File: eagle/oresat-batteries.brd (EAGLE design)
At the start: 94 x 93.5 mm, 62 parts, among them IC1 74AHC1G08DBV, U1 TCAN330, U2 STM32F042K6, X1 16MHz

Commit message: More cleaning.
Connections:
- removed net N$4: CF1.P$1, D2.3
- new net BATOUT: CF1.P$3, D2.3
- net CANH: now also CF1.P$2; no longer CF1.P$4
- net CANL: now also CF1.P$1; no longer CF1.P$5
- net ISO_S: now also CF1.P$5; no longer CF1.P$2
- net VSOLAR: now also CF1.P$4; no longer CF1.P$3
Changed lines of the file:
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@@
 <wire x1="17.35" y1="76" x2="21.85" y2="81.93" width="0" layer="19" extent="1-1"/>
-</signal>
-<signal name="LEDNP">
-<contactref element="R2" pad="2"/>
-<contactref element="LED1" pad="A"/>
-<wire x1="13.35" y1="76" x2="28.5" y2="76.75" width="0" layer="19" extent="1-1"/>
 </signal>
 <signal name="ADP_LED">
@@
 <signal name="ISO_S">
 <contactref element="C3" pad="1"/>
-<contactref element="CF1" pad="P$2"/>
 <contactref element="U$1" pad="9"/>
 <contactref element="U$1" pad="11"/>
 <contactref element="U$1" pad="10"/>
+<contactref element="CF1" pad="P$5"/>
 <wire x1="22.85" y1="78.23" x2="23.7" y2="79.08" width="0" layer="19" extent="1-1"/>
 <wire x1="22.35" y1="78.23" x2="22.85" y2="78.23" width="0" layer="19" extent="1-1"/>
 <wire x1="11.65" y1="73" x2="22.35" y2="78.23" width="0" layer="19" extent="1-1"/>
-<wire x1="9.435" y1="92.04" x2="22.35" y2="78.23" width="0" layer="19" extent="1-1"/>
+<wire x1="11.975" y1="86.96" x2="22.35" y2="78.23" width="0" layer="19" extent="1-1"/>
 </signal>
 <signal name="VSOLAR">
+<contactref element="DEBUG_DNP" pad="7"/>
+<contactref element="DEBUG_DNP" pad="8"/>
 <contactref element="U$1" pad="8"/>
 <contactref element="U$1" pad="6"/>
 <contactref element="U$1" pad="7"/>
-<contactref element="CF1" pad="P$3"/>
 <contactref element="C5" pad="1"/>
-<contactref element="DEBUG_DNP" pad="7"/>
-<contactref element="DEBUG_DNP" pad="8"/>
-<wire x1="21.35" y1="78.23" x2="21.85" y2="78.23" width="0" layer="19" extent="1-1"/>
-<wire x1="20.85" y1="78.23" x2="21.35" y2="78.23" width="0" layer="19" extent="1-1"/>
-<wire x1="10.705" y1="86.96" x2="20.85" y2="78.23" width="0" layer="19" extent="1-1"/>
+<contactref element="CF1" pad="P$4"/>
+<wire x1="20.85" y1="78.23" x2="10.705" y2="92.04" width="0" layer="19" extent="1-1"/>
+<wire x1="21.35" y1="78.23" x2="20.85" y2="78.23" width="0" layer="19" extent="1-1"/>
+<wire x1="21.85" y1="78.23" x2="21.35" y2="78.23" width="0" layer="19" extent="1-1"/>
 <wire x1="19.15" y1="52.5" x2="20.85" y2="78.23" width="0" layer="19" extent="1-1"/>
 <wire x1="0.23" y1="-13.73" x2="19.15" y2="52.5" width="0" layer="19" extent="1-1"/>
@@
 <contactref element="R7" pad="1"/>
 <contactref element="U$2" pad="5"/>
-<contactref element="CF1" pad="P$6"/>
 <contactref element="IC1" pad="1"/>
 <contactref element="R14" pad="2"/>
+<contactref element="CF1" pad="P$6"/>
 <wire x1="15.65" y1="73" x2="26.66" y2="77.875" width="0" layer="19" extent="1-1"/>
 <wire x1="9.35" y1="79" x2="15.65" y2="73" width="0" layer="19" extent="1-1"/>
@@
 <wire x1="16.35" y1="56.5" x2="15" y2="66.75" width="0" layer="19" extent="1-1"/>
 </signal>
-<signal name="N$4">
-<contactref element="CF1" pad="P$1"/>
-<contactref element="D2" pad="3"/>
-<wire x1="15.5" y1="47.4" x2="9.435" y2="86.96" width="0" layer="19" extent="1-1"/>
-</signal>
 <signal name="IO0">
 <contactref element="U$5" pad="1"/>
@@
 <signal name="CANH">
 <contactref element="U1" pad="7"/>
-<contactref element="CF1" pad="P$4"/>
 <contactref element="DEBUG_DNP" pad="14"/>
 <contactref element="DEBUG_DNP" pad="13"/>
-<wire x1="27.175" y1="74.8" x2="10.705" y2="92.04" width="0" layer="19" extent="1-1"/>
+<contactref element="CF1" pad="P$2"/>
+<wire x1="9.435" y1="92.04" x2="27.175" y2="74.8" width="0" layer="19" extent="1-1"/>
 <wire x1="7.85" y1="-13.73" x2="27.175" y2="74.8" width="0" layer="19" extent="1-1"/>
 <wire x1="7.85" y1="-16.27" x2="7.85" y2="-13.73" width="0" layer="19" extent="1-1"/>
@@
 <signal name="CANL">
 <contactref element="U1" pad="6"/>
-<contactref element="CF1" pad="P$5"/>
 <contactref element="DEBUG_DNP" pad="12"/>
 <contactref element="DEBUG_DNP" pad="11"/>
-<wire x1="11.975" y1="86.96" x2="27.825" y2="74.8" width="0" layer="19" extent="1-1"/>
+<contactref element="CF1" pad="P$1"/>
+<wire x1="9.435" y1="86.96" x2="27.825" y2="74.8" width="0" layer="19" extent="1-1"/>
 <wire x1="5.31" y1="-13.73" x2="27.825" y2="74.8" width="0" layer="19" extent="1-1"/>
 <wire x1="5.31" y1="-16.27" x2="5.31" y2="-13.73" width="0" layer="19" extent="1-1"/>
@@
 </signal>
 <signal name="VBATT+">
-<contactref element="U$1" pad="4"/>
-<contactref element="U$1" pad="12"/>
-<contactref element="U$1" pad="13"/>
-<contactref element="U$1" pad="14"/>
 <contactref element="C2" pad="1"/>
 <contactref element="U2" pad="17"/>
@@
 <contactref element="C11" pad="1"/>
 <contactref element="U2" pad="1"/>
-<contactref element="CF2" pad="2"/>
 <contactref element="U1" pad="3"/>
 <contactref element="C13" pad="1"/>
@@
 <contactref element="R7" pad="2"/>
 <contactref element="R10" pad="2"/>
+<contactref element="U$1" pad="4"/>
+<contactref element="U$1" pad="12"/>
+<contactref element="U$1" pad="13"/>
+<contactref element="U$1" pad="14"/>
+<contactref element="CF2" pad="2"/>
 <wire x1="23.7" y1="80.08" x2="23.7" y2="79.58" width="0" layer="19" extent="1-1"/>
 <wire x1="23.7" y1="80.58" x2="23.7" y2="80.08" width="0" layer="19" extent="1-1"/>
@@
 <wire x1="-4.475" y1="-3.435" x2="-3.825" y2="-3.435" width="0" layer="19" extent="1-1"/>
 </signal>
+<signal name="LEDNP">
+<contactref element="R2" pad="2"/>
+<contactref element="LED1" pad="A"/>
+<wire x1="13.35" y1="76" x2="28.5" y2="76.75" width="0" layer="19" extent="1-1"/>
+</signal>
+<signal name="BATOUT">
+<contactref element="D2" pad="3"/>
+<contactref element="CF1" pad="P$3"/>
+<wire x1="15.5" y1="47.4" x2="10.705" y2="86.96" width="0" layer="19" extent="1-1"/>
+</signal>
 </signals>

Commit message: Fixed V- pin on STC
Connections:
- net C_SENSE: no longer R6.2
- net GND: now also R6.2
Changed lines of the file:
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@@
 <contactref element="C14" pad="2"/>
 <contactref element="R3" pad="1"/>
+<contactref element="R6" pad="2"/>
 <wire x1="21.85" y1="80.08" x2="20.85" y2="81.93" width="0" layer="19" extent="1-1"/>
 <wire x1="22.415" y1="75.42" x2="21.85" y2="80.08" width="0" layer="19" extent="1-1"/>
@@
 <wire x1="14.2" y1="66.75" x2="13.35" y2="70" width="0" layer="19" extent="1-1"/>
 <wire x1="11.65" y1="76" x2="13.35" y2="73" width="0" layer="19" extent="1-1"/>
-<wire x1="7.65" y1="73" x2="11.65" y2="76" width="0" layer="19" extent="1-1"/>
+<wire x1="9.35" y1="76" x2="11.65" y2="76" width="0" layer="19" extent="1-1"/>
+<wire x1="7.65" y1="73" x2="9.35" y2="76" width="0" layer="19" extent="1-1"/>
 <wire x1="27.175" y1="72.2" x2="22.415" y2="75.42" width="0" layer="19" extent="1-1"/>
 <wire x1="24.85" y1="68.5" x2="27.175" y2="72.2" width="0" layer="19" extent="1-1"/>
@@
 </signal>
 <signal name="C_SENSE">
-<contactref element="R6" pad="2"/>
 <contactref element="R3" pad="2"/>
 <contactref element="U$13" pad="P$1"/>
@@
 <contactref element="U$13" pad="P$3"/>
 <contactref element="U$5" pad="6"/>
-<wire x1="9.35" y1="76" x2="21.795" y2="75.42" width="0" layer="19" extent="1-1"/>
 <wire x1="29.35" y1="53" x2="21.795" y2="75.42" width="0" layer="19" extent="1-1"/>
 <wire x1="-3.175" y1="-3.435" x2="29.35" y2="53" width="0" layer="19" extent="1-1"/>

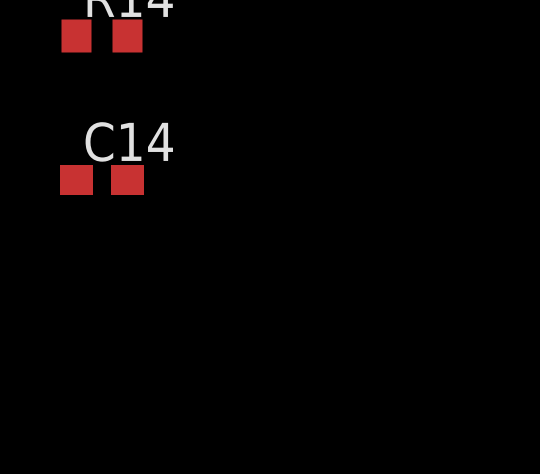
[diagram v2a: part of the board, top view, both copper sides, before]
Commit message: Fixed TP non-connect issue
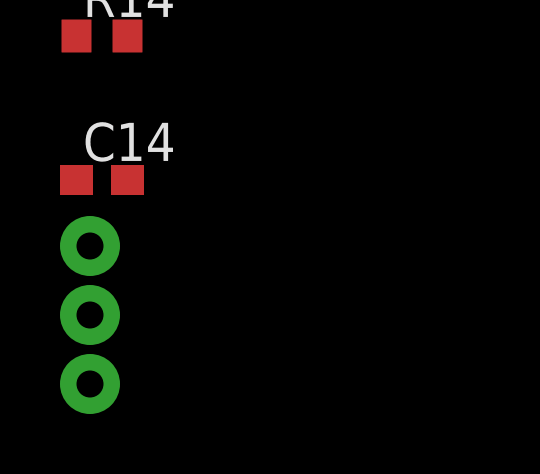
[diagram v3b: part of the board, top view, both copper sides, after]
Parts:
- added U$18, U$19, U$28: TP, oresat-batteries:2MM_TP
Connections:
- net BQBAT: now also U$26.P$1, U$4.P$1
- net CANH: now also U$12.P$1
- net CANL: now also U$8.P$1
- net COUT: now also U$19.P$1
- net C_SENSE: now also U$18.P$1
- net GND: now also U$16.P$1, U$17.P$1, U$22.P$1, U$23.P$1
- net IO0: now also U$9.P$1
- net N$5: now also U$28.P$1
- net NRESET: now also U$25.P$1
- net PA8: now also U$27.P$1
- net SCL: now also U$10.P$1
- net SDA: now also U$11.P$1
- net SYS_EN: now also U$24.P$1
- net VBATT+: now also U$15.P$1, U$7.P$1
- net VSOLAR: now also U$6.P$1
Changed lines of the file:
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@@
 <element name="R14" library="rcl" package="R0603" value="2.2k" x="-29.4" y="-44.6"/>
 <element name="C14" library="rcl" package="C0603" value="" x="-29.4" y="-49.4"/>
+<element name="U$18" library="oresat-batteries" package="2MM_TP" value="TP" x="-29.8" y="-51.6"/>
+<element name="U$19" library="oresat-batteries" package="2MM_TP" value="TP" x="-29.8" y="-53.9"/>
+<element name="U$28" library="oresat-batteries" package="2MM_TP" value="TP" x="-29.8" y="-56.2"/>
 </elements>
 <signals>
@@
 <contactref element="R3" pad="1"/>
 <contactref element="R6" pad="2"/>
+<contactref element="U$22" pad="P$1"/>
+<contactref element="U$23" pad="P$1"/>
+<contactref element="U$16" pad="P$1"/>
+<contactref element="U$17" pad="P$1"/>
 <wire x1="21.85" y1="80.08" x2="20.85" y2="81.93" width="0" layer="19" extent="1-1"/>
 <wire x1="22.415" y1="75.42" x2="21.85" y2="80.08" width="0" layer="19" extent="1-1"/>
@@
 <wire x1="10.39" y1="-13.73" x2="32.5" y2="21" width="0" layer="19" extent="16-16"/>
 <wire x1="10.39" y1="-16.27" x2="10.39" y2="-13.73" width="0" layer="19" extent="1-1"/>
-<wire x1="-26.95" y1="-39.09" x2="10.39" y2="-16.27" width="0" layer="19" extent="1-1"/>
+<wire x1="-8" y1="-9" x2="10.39" y2="-13.73" width="0" layer="19" extent="1-1"/>
+<wire x1="-8" y1="-6.5" x2="-8" y2="-9" width="0" layer="19" extent="1-1"/>
+<wire x1="-21.5" y1="-29" x2="-8" y2="-9" width="0" layer="19" extent="1-1"/>
+<wire x1="-21.5" y1="-31.5" x2="-21.5" y2="-29" width="0" layer="19" extent="1-1"/>
+<wire x1="-26.95" y1="-39.09" x2="-21.5" y2="-31.5" width="0" layer="19" extent="1-1"/>
 <wire x1="-28.55" y1="-49.4" x2="-26.95" y2="-39.09" width="0" layer="19" extent="1-1"/>
 </signal>
@@
 <contactref element="C5" pad="1"/>
 <contactref element="CF1" pad="P$4"/>
+<contactref element="U$6" pad="P$1"/>
 <wire x1="20.85" y1="78.23" x2="10.705" y2="92.04" width="0" layer="19" extent="1-1"/>
 <wire x1="21.35" y1="78.23" x2="20.85" y2="78.23" width="0" layer="19" extent="1-1"/>
 <wire x1="21.85" y1="78.23" x2="21.35" y2="78.23" width="0" layer="19" extent="1-1"/>
-<wire x1="19.15" y1="52.5" x2="20.85" y2="78.23" width="0" layer="19" extent="1-1"/>
+<wire x1="34" y1="66.5" x2="21.85" y2="78.23" width="0" layer="19" extent="1-1"/>
+<wire x1="19.15" y1="52.5" x2="34" y2="66.5" width="0" layer="19" extent="1-1"/>
 <wire x1="0.23" y1="-13.73" x2="19.15" y2="52.5" width="0" layer="19" extent="1-1"/>
 <wire x1="0.23" y1="-16.27" x2="0.23" y2="-13.73" width="0" layer="19" extent="1-1"/>
@@
 <contactref element="R14" pad="2"/>
 <contactref element="CF1" pad="P$6"/>
+<contactref element="U$4" pad="P$1"/>
+<contactref element="U$26" pad="P$1"/>
+<wire x1="34" y1="69" x2="26.66" y2="77.875" width="0" layer="19" extent="1-1"/>
 <wire x1="15.65" y1="73" x2="26.66" y2="77.875" width="0" layer="19" extent="1-1"/>
 <wire x1="9.35" y1="79" x2="15.65" y2="73" width="0" layer="19" extent="1-1"/>
 <wire x1="11.975" y1="92.04" x2="9.35" y2="79" width="0" layer="19" extent="1-1"/>
-<wire x1="-28.85" y1="-39.09" x2="15.65" y2="73" width="0" layer="19" extent="1-1"/>
+<wire x1="-21.8" y1="-38.8" x2="15.65" y2="73" width="0" layer="19" extent="1-1"/>
+<wire x1="-28.85" y1="-39.09" x2="-21.8" y2="-38.8" width="0" layer="19" extent="1-1"/>
 <wire x1="-28.55" y1="-44.6" x2="-28.85" y2="-39.09" width="0" layer="19" extent="1-1"/>
 </signal>
@@
 <contactref element="CF2" pad="3"/>
 <contactref element="U2" pad="4"/>
+<contactref element="U$25" pad="P$1"/>
 <wire x1="4.25" y1="56.5" x2="12.75" y2="62.9" width="0" layer="19" extent="1-1"/>
+<wire x1="-21.5" y1="-36.5" x2="4.25" y2="56.5" width="0" layer="19" extent="1-1"/>
 </signal>
 <signal name="SDA">
@@
 <contactref element="U2" pad="30"/>
 <contactref element="R8" pad="1"/>
+<contactref element="U$11" pad="P$1"/>
 <wire x1="21.795" y1="71.61" x2="22.35" y2="81.93" width="0" layer="19" extent="1-1"/>
 <wire x1="15.8" y1="66.75" x2="21.795" y2="71.61" width="0" layer="19" extent="1-1"/>
 <wire x1="27.65" y1="64.5" x2="21.795" y2="71.61" width="0" layer="19" extent="1-1"/>
+<wire x1="34" y1="56.5" x2="27.65" y2="64.5" width="0" layer="19" extent="1-1"/>
 </signal>
 <signal name="SCL">
@@
 <contactref element="U$5" pad="4"/>
 <contactref element="R9" pad="1"/>
+<contactref element="U$10" pad="P$1"/>
 <wire x1="22.415" y1="71.61" x2="20" y2="81.08" width="0" layer="19" extent="1-1"/>
 <wire x1="16.6" y1="66.75" x2="22.415" y2="71.61" width="0" layer="19" extent="1-1"/>
 <wire x1="27.65" y1="60.5" x2="22.415" y2="71.61" width="0" layer="19" extent="1-1"/>
+<wire x1="34" y1="59" x2="27.65" y2="60.5" width="0" layer="19" extent="1-1"/>
 </signal>
 <signal name="STC_IO">
@@
 <contactref element="R10" pad="1"/>
 <contactref element="R13" pad="2"/>
+<contactref element="U$9" pad="P$1"/>
+<wire x1="34" y1="61.5" x2="29.35" y2="68.5" width="0" layer="19" extent="1-1"/>
 <wire x1="20.555" y1="71.61" x2="29.35" y2="68.5" width="0" layer="19" extent="1-1"/>
-<wire x1="23.15" y1="57" x2="29.35" y2="68.5" width="0" layer="19" extent="1-1"/>
+<wire x1="23.15" y1="57" x2="34" y2="61.5" width="0" layer="19" extent="1-1"/>
 </signal>
 <signal name="CANH">
@@
 <contactref element="DEBUG_DNP" pad="13"/>
 <contactref element="CF1" pad="P$2"/>
+<contactref element="U$12" pad="P$1"/>
 <wire x1="9.435" y1="92.04" x2="27.175" y2="74.8" width="0" layer="19" extent="1-1"/>
-<wire x1="7.85" y1="-13.73" x2="27.175" y2="74.8" width="0" layer="19" extent="1-1"/>
+<wire x1="1.5" y1="-4" x2="27.175" y2="74.8" width="0" layer="19" extent="1-1"/>
+<wire x1="7.85" y1="-13.73" x2="1.5" y2="-4" width="0" layer="19" extent="1-1"/>
 <wire x1="7.85" y1="-16.27" x2="7.85" y2="-13.73" width="0" layer="19" extent="1-1"/>
 </signal>
@@
 <contactref element="DEBUG_DNP" pad="11"/>
 <contactref element="CF1" pad="P$1"/>
+<contactref element="U$8" pad="P$1"/>
 <wire x1="9.435" y1="86.96" x2="27.825" y2="74.8" width="0" layer="19" extent="1-1"/>
-<wire x1="5.31" y1="-13.73" x2="27.825" y2="74.8" width="0" layer="19" extent="1-1"/>
+<wire x1="1.5" y1="-1.5" x2="27.825" y2="74.8" width="0" layer="19" extent="1-1"/>
+<wire x1="5.31" y1="-13.73" x2="1.5" y2="-1.5" width="0" layer="19" extent="1-1"/>
 <wire x1="5.31" y1="-16.27" x2="5.31" y2="-13.73" width="0" layer="19" extent="1-1"/>
 </signal>
@@
 <contactref element="U$1" pad="14"/>
 <contactref element="CF2" pad="2"/>
+<contactref element="U$7" pad="P$1"/>
+<contactref element="U$15" pad="P$1"/>
 <wire x1="23.7" y1="80.08" x2="23.7" y2="79.58" width="0" layer="19" extent="1-1"/>
 <wire x1="23.7" y1="80.58" x2="23.7" y2="80.08" width="0" layer="19" extent="1-1"/>
@@
 <wire x1="29.35" y1="60.5" x2="24.85" y2="57" width="0" layer="19" extent="1-1"/>
 <wire x1="29.35" y1="64.5" x2="29.35" y2="60.5" width="0" layer="19" extent="1-1"/>
+<wire x1="34" y1="64" x2="29.35" y2="64.5" width="0" layer="19" extent="1-1"/>
 <wire x1="16.45" y1="49.6" x2="23.15" y2="53" width="0" layer="19" extent="1-1"/>
+<wire x1="34" y1="54" x2="29.35" y2="60.5" width="0" layer="19" extent="1-1"/>
 <wire x1="12.75" y1="62.1" x2="21.25" y2="59.7" width="0" layer="19" extent="1-1"/>
 <wire x1="12.75" y1="65.3" x2="12.75" y2="62.1" width="0" layer="19" extent="1-1"/>
 <wire x1="9.35" y1="70" x2="12.75" y2="65.3" width="0" layer="19" extent="1-1"/>
 <wire x1="4.25" y1="54.5" x2="12.75" y2="62.1" width="0" layer="19" extent="1-1"/>
-<wire x1="45" y1="14.5" x2="23.15" y2="53" width="0" layer="19" extent="1-16"/>
+<wire x1="45" y1="14.5" x2="34" y2="54" width="0" layer="19" extent="16-16"/>
 <wire x1="-7.39" y1="-13.73" x2="45" y2="14.5" width="0" layer="19" extent="16-16"/>
 <wire x1="-7.39" y1="-16.27" x2="-7.39" y2="-13.73" width="0" layer="19" extent="1-1"/>
@@
 <contactref element="U2" pad="14"/>
 <contactref element="U$1" pad="16"/>
+<contactref element="U$24" pad="P$1"/>
 <wire x1="18.2" y1="58.25" x2="22.85" y2="81.93" width="0" layer="19" extent="1-1"/>
+<wire x1="-21.5" y1="-34" x2="18.2" y2="58.25" width="0" layer="19" extent="1-1"/>
 </signal>
 <signal name="DIG_IO1">
@@
 <signal name="PA8">
 <contactref element="U2" pad="18"/>
+<contactref element="U$27" pad="P$1"/>
+<wire x1="-21.8" y1="-41.1" x2="21.25" y2="60.5" width="0" layer="19" extent="1-1"/>
 </signal>
 <signal name="ANDDRIVE">
@@
 <contactref element="U$2" pad="3"/>
 <contactref element="IC1" pad="2"/>
+<contactref element="U$28" pad="P$1"/>
 <wire x1="-27.9" y1="-39.09" x2="27.16" y2="76.825" width="0" layer="19" extent="1-1"/>
+<wire x1="-29.8" y1="-56.2" x2="-27.9" y2="-39.09" width="0" layer="19" extent="1-1"/>
 </signal>
 <signal name="N$6">
@@
 <contactref element="U$13" pad="P$4"/>
 <contactref element="U$2" pad="2"/>
+<contactref element="U$19" pad="P$1"/>
 <wire x1="-2.525" y1="-3.435" x2="26.66" y2="76.825" width="0" layer="19" extent="1-1"/>
+<wire x1="-29.8" y1="-53.9" x2="-2.525" y2="-3.435" width="0" layer="19" extent="1-1"/>
 </signal>
 <signal name="C_SENSE">
@@
 <contactref element="U$13" pad="P$3"/>
 <contactref element="U$5" pad="6"/>
+<contactref element="U$18" pad="P$1"/>
 <wire x1="29.35" y1="53" x2="21.795" y2="75.42" width="0" layer="19" extent="1-1"/>
 <wire x1="-3.175" y1="-3.435" x2="29.35" y2="53" width="0" layer="19" extent="1-1"/>
 <wire x1="-3.825" y1="-3.435" x2="-3.175" y2="-3.435" width="0" layer="19" extent="1-1"/>
 <wire x1="-4.475" y1="-3.435" x2="-3.825" y2="-3.435" width="0" layer="19" extent="1-1"/>
+<wire x1="-29.8" y1="-51.6" x2="-4.475" y2="-3.435" width="0" layer="19" extent="1-1"/>
 </signal>
 <signal name="LEDNP">
